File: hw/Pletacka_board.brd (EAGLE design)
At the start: 75 x 55 mm, 52 parts, among them U1 LM75BDP-NEW, U2 EL357N(A)(TA)-G, U3 EL357N(A)(TA)-G, U4 EL357N(A)(TA)-G, U5 EL357N(A)(TA)-G, U6 TPS54231D

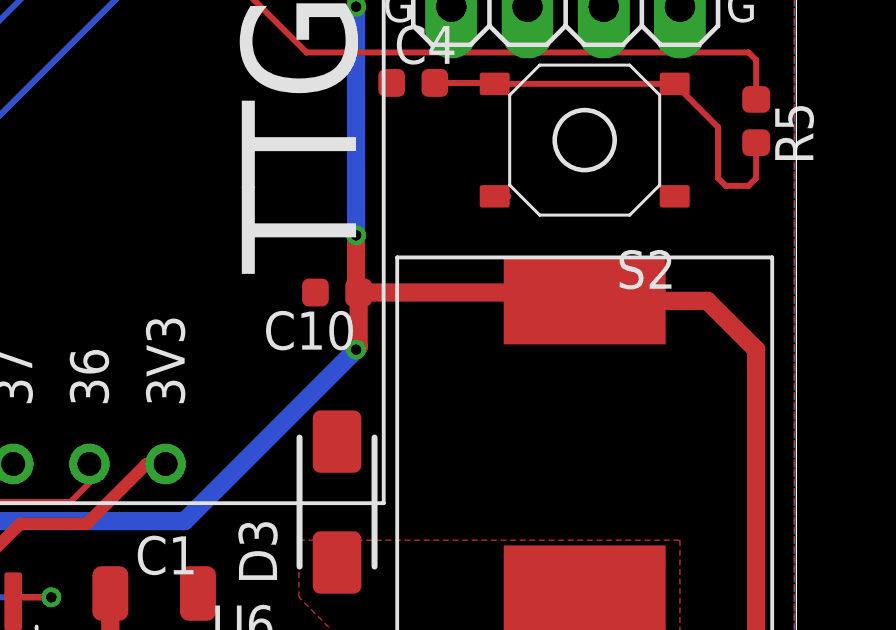
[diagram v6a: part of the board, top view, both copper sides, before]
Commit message: Change package of capacitor to 0805 (close #3)
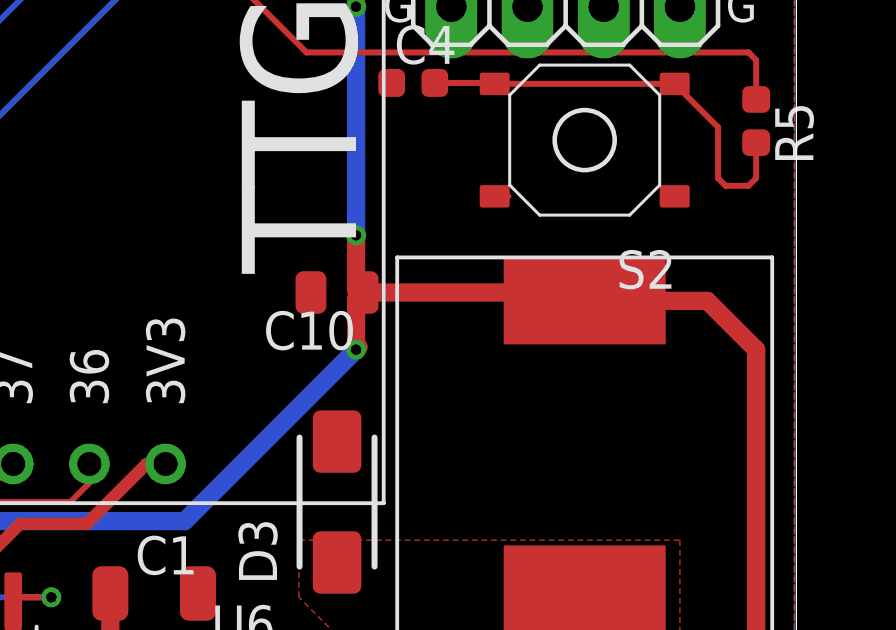
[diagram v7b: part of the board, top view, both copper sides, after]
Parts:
- C10: device rcl_upravena:C0603 -> rcl_upravena:C0805
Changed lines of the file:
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@@
 <attribute name="VALUE" x="67.31" y="17.78" size="1.27" layer="27" rot="R180"/>
 </element>
-<element name="C10" library="rcl_upravena" package="C0603" value="22u" x="59.69" y="31.115" smashed="yes" rot="R180">
-<attribute name="LCSC_ID" value="C59461" x="59.69" y="31.115" size="1.778" layer="27" rot="R180" display="off"/>
+<element name="C10" library="rcl_upravena" package="C0805" value="22u" x="59.69" y="31.115" smashed="yes" rot="R180">
+<attribute name="LCSC_ID" value="C45783" x="59.69" y="31.115" size="1.778" layer="27" rot="R180" display="off"/>
 <attribute name="NAME" x="60.325" y="30.48" size="1.27" layer="25" rot="R180"/>
 <attribute name="VALUE" x="60.325" y="33.02" size="1.27" layer="27" rot="R180"/>
@@
 <vertex x="0" y="0"/>
 </polygon>
-<wire x1="59.055" y1="31.03" x2="58.97" y2="31.115" width="0.1524" layer="1"/>
 <via x="59.055" y="17.145" extent="1-16" drill="0.65"/>
 <via x="59.055" y="15.24" extent="1-16" drill="0.65"/>
@@
 <via x="61.595" y="13.335" extent="1-16" drill="0.65"/>
 <via x="56.515" y="13.335" extent="1-16" drill="0.65"/>
+<wire x1="53.975" y1="48.26" x2="63.5" y2="52.705" width="0" layer="19" extent="1-1"/>
+<wire x1="51.435" y1="48.26" x2="53.975" y2="48.26" width="0" layer="19" extent="1-1"/>
+<wire x1="63.5" y1="40.64" x2="63.5" y2="52.705" width="0" layer="19" extent="1-1"/>
+<wire x1="66.04" y1="40.64" x2="63.5" y2="40.64" width="0" layer="19" extent="1-1"/>
+<wire x1="68.58" y1="40.64" x2="66.04" y2="40.64" width="0" layer="19" extent="1-1"/>
+<wire x1="71.12" y1="40.64" x2="68.58" y2="40.64" width="0" layer="19" extent="1-1"/>
+<wire x1="61.51" y1="38.1" x2="63.5" y2="40.64" width="0" layer="19" extent="1-1"/>
+<wire x1="64.945" y1="34.32" x2="61.51" y2="37.755" width="0" layer="19" extent="1-1"/>
+<wire x1="70.945" y1="34.32" x2="65.405" y2="34.32" width="0" layer="19" extent="1-1"/>
+<wire x1="58.82" y1="31.115" x2="64.945" y2="34.32" width="0" layer="19" extent="1-1"/>
+<wire x1="59.69" y1="26.145" x2="58.82" y2="31.115" width="0" layer="19" extent="1-1"/>
+<wire x1="55.054" y1="21.082" x2="59.69" y2="26.145" width="0" layer="19" extent="1-1"/>
+<wire x1="50.165" y1="20.955" x2="55.054" y2="21.082" width="0" layer="19" extent="1-1"/>
+<wire x1="28.575" y1="25.4" x2="28.575" y2="20.82" width="0" layer="19" extent="1-1"/>
+<wire x1="59.055" y1="17.145" x2="55.054" y2="21.082" width="0" layer="19" extent="1-1"/>
+<wire x1="61.525" y1="17.145" x2="59.055" y2="17.145" width="0" layer="19" extent="1-1"/>
+<wire x1="64.05" y1="17.145" x2="61.525" y2="17.145" width="0" layer="19" extent="1-1"/>
+<wire x1="61.595" y1="13.335" x2="59.055" y2="13.335" width="0" layer="19" extent="1-1"/>
+<wire x1="56.515" y1="13.335" x2="53.975" y2="13.25" width="0" layer="19" extent="1-1"/>
+<wire x1="2.032" y1="33.232" x2="2.08" y2="26.065" width="0" layer="19" extent="1-1"/>
+<wire x1="2.905" y1="42.103" x2="3.175" y2="34.925" width="0" layer="19" extent="1-1"/>
+<wire x1="2.905" y1="42.855" x2="2.905" y2="43.505" width="0" layer="19" extent="1-1"/>
+<wire x1="1.905" y1="45.1104" x2="2.905" y2="43.505" width="0" layer="19" extent="1-1"/>
+<wire x1="7.255" y1="44.257" x2="2.905" y2="43.505" width="0" layer="19" extent="1-1"/>
+<wire x1="31.115" y1="48.26" x2="51.435" y2="48.26" width="0" layer="19" extent="1-1"/>
+<wire x1="28.575" y1="48.26" x2="31.115" y2="48.26" width="0" layer="19" extent="1-1"/>
 </signal>
 <signal name="+3V3">
@@
 <wire x1="72.035" y1="30.835" x2="73.66" y2="29.21" width="0.6096" layer="1"/>
 <wire x1="73.66" y1="29.21" x2="73.66" y2="14.605" width="0.6096" layer="1"/>
-<wire x1="60.41" y1="31.115" x2="68.3" y2="31.115" width="0.6096" layer="1"/>
+<wire x1="60.56" y1="31.115" x2="68.3" y2="31.115" width="0.6096" layer="1"/>
 <wire x1="68.3" y1="31.115" x2="68.58" y2="30.835" width="0.6096" layer="1"/>
-<wire x1="60.41" y1="31.115" x2="60.41" y2="29.295" width="0.6096" layer="1"/>
 <wire x1="60.41" y1="29.295" x2="60.325" y2="29.21" width="0.6096" layer="1"/>
 <via x="60.325" y="29.21" extent="1-16" drill="0.35"/>
@@
 <wire x1="54.61" y1="23.495" x2="27.94" y2="23.495" width="0.6096" layer="16"/>
 <contactref element="JP1" pad="3"/>
-<wire x1="60.41" y1="31.115" x2="60.325" y2="31.2" width="0.6096" layer="1"/>
 <wire x1="60.325" y1="31.2" x2="60.325" y2="33.02" width="0.6096" layer="1"/>
 <via x="60.325" y="33.02" extent="1-16" drill="0.35"/>
@@
 <wire x1="60.325" y1="44.45" x2="60.325" y2="40.64" width="0.6096" layer="1"/>
 <wire x1="60.325" y1="44.45" x2="63.5" y2="47.625" width="0.6096" layer="1"/>
+<wire x1="60.325" y1="29.21" x2="60.325" y2="30.88" width="0.6096" layer="1"/>
+<wire x1="60.325" y1="30.88" x2="60.56" y2="31.115" width="0.6096" layer="1"/>
+<wire x1="60.56" y1="31.115" x2="60.325" y2="31.2" width="0" layer="19" extent="1-1"/>
 </signal>
 <signal name="TMP_SDA">

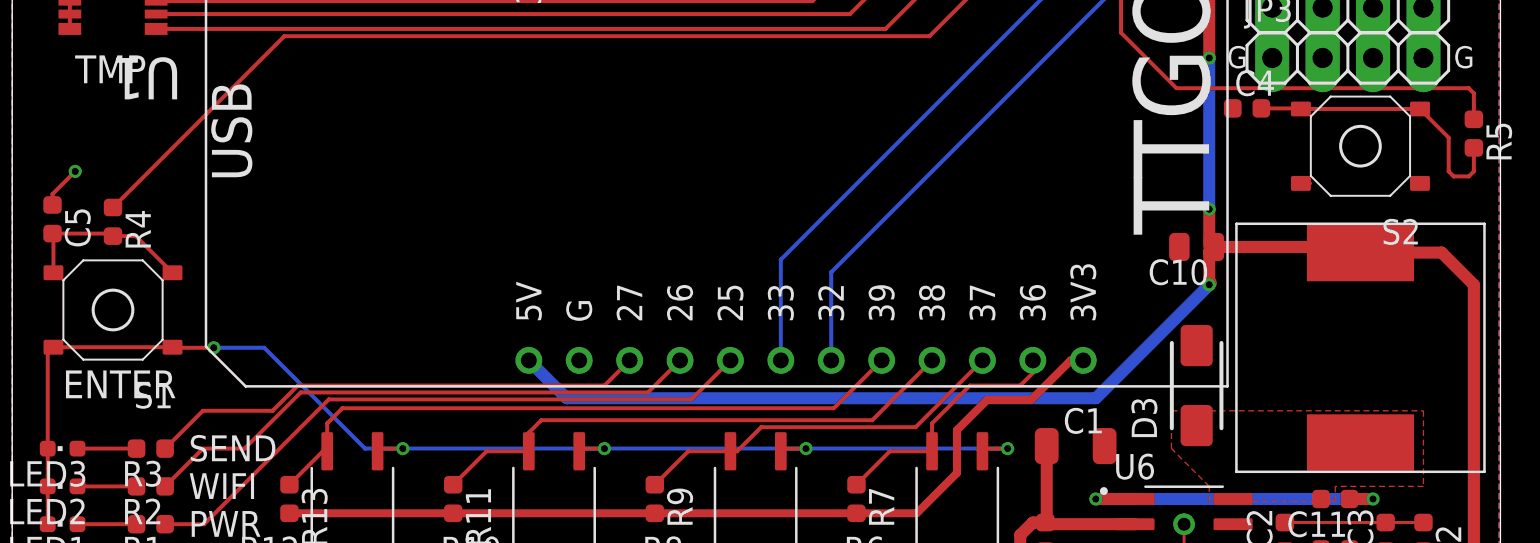
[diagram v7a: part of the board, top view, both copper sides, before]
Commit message: Edit buttons lables (close #16)
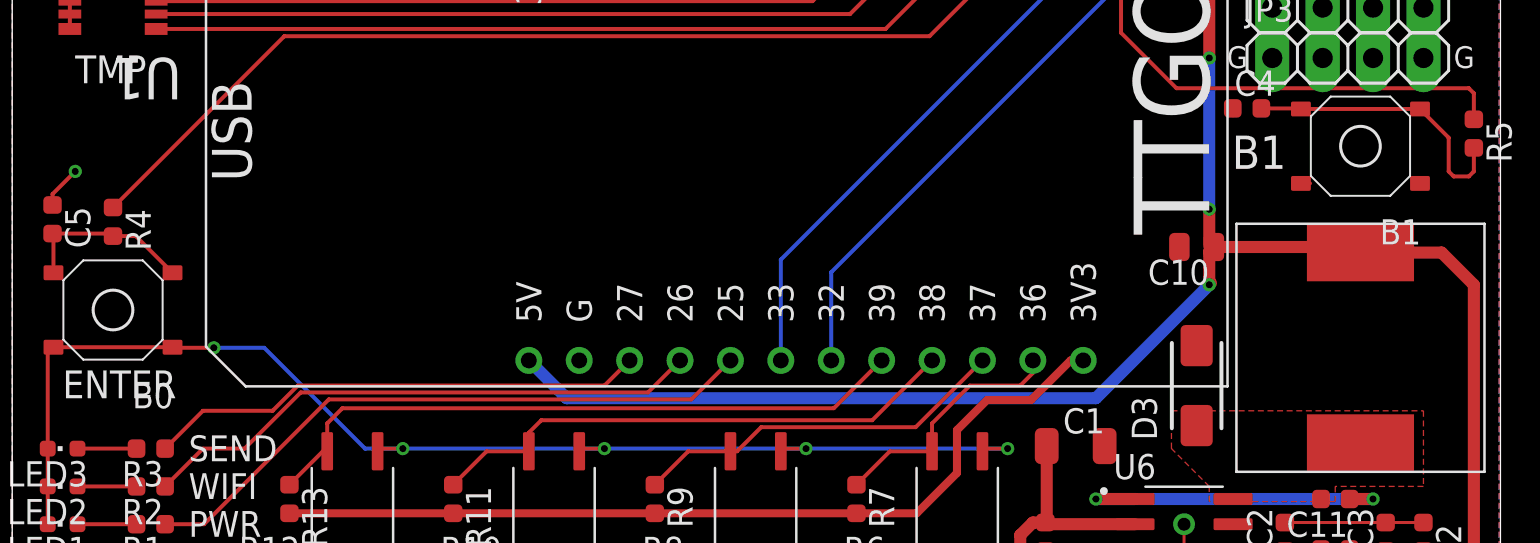
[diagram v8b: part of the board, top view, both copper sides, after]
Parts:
- B0: value CHOOSE_ME -> ENTER
- B1: value CHOOSE_ME -> B1
- renumbered S1 to B0, S2 to B1
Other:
- board text added: "B1"
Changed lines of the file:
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@@
 <drawing>
 <settings>
-<setting alwaysvectorfont="no"/>
+<setting alwaysvectorfont="yes"/>
 <setting verticaltext="up"/>
 </settings>
@@
 <text x="72.644" y="40.132" size="1.1" layer="21" font="vector" ratio="20" rot="SR0">G</text>
 <text x="61.214" y="40.132" size="1.1" layer="21" font="vector" ratio="20" rot="SR0">G</text>
+<text x="61.468" y="35.052" size="1.6764" layer="21" font="vector" ratio="20" rot="SR0">B1</text>
 </plain>
 <attributes>
@@
 <attribute name="LCSC_ID" value="C169399" x="67.945" y="26.035" size="1.778" layer="27" rot="R90" display="off"/>
 </element>
-<element name="S1" library="switch-omron" package="TS-1187A" value="CHOOSE_ME" x="5.08" y="27.94" smashed="yes" rot="R180">
+<element name="B0" library="switch-omron" package="TS-1187A" value="ENTER" x="5.08" y="27.94" smashed="yes" rot="R180">
 <attribute name="LCSC_ID" value="C318888" x="5.08" y="27.94" size="1.778" layer="27" rot="R180" display="off"/>
 <attribute name="NAME" x="8.128" y="24.257" size="1.27" layer="25" ratio="10" rot="R180"/>
 <attribute name="VALUE" x="8.128" y="33.02" size="1.27" layer="27" ratio="10" rot="R180"/>
 </element>
-<element name="S2" library="switch-omron" package="TS-1187A" value="CHOOSE_ME" x="67.945" y="36.195" smashed="yes" rot="R180">
+<element name="B1" library="switch-omron" package="TS-1187A" value="B1" x="67.945" y="36.195" smashed="yes" rot="R180">
 <attribute name="LCSC_ID" value="C318888" x="67.945" y="36.195" size="1.778" layer="27" rot="R180" display="off"/>
 <attribute name="NAME" x="70.993" y="32.512" size="1.27" layer="25" ratio="10" rot="R180"/>
@@
 <contactref element="U1" pad="5"/>
 <contactref element="C5" pad="1"/>
-<contactref element="S1" pad="A"/>
-<contactref element="S1" pad="B"/>
-<contactref element="S2" pad="A"/>
-<contactref element="S2" pad="B"/>
+<contactref element="B0" pad="A"/>
+<contactref element="B0" pad="B"/>
+<contactref element="B1" pad="A"/>
+<contactref element="B1" pad="B"/>
 <polygon width="0.6096" layer="1" rank="2">
 <vertex x="0" y="55"/>
@@
 <vertex x="0" y="0"/>
 </polygon>
+<wire x1="59.055" y1="31.03" x2="58.82" y2="31.115" width="0.1524" layer="1"/>
 <via x="59.055" y="17.145" extent="1-16" drill="0.65"/>
 <via x="59.055" y="15.24" extent="1-16" drill="0.65"/>
@@
 <wire x1="64.945" y1="34.32" x2="61.51" y2="37.755" width="0" layer="19" extent="1-1"/>
 <wire x1="70.945" y1="34.32" x2="65.405" y2="34.32" width="0" layer="19" extent="1-1"/>
-<wire x1="58.82" y1="31.115" x2="64.945" y2="34.32" width="0" layer="19" extent="1-1"/>
-<wire x1="59.69" y1="26.145" x2="58.82" y2="31.115" width="0" layer="19" extent="1-1"/>
+<wire x1="59.055" y1="31.03" x2="64.945" y2="34.32" width="0" layer="19" extent="1-1"/>
+<wire x1="59.69" y1="26.145" x2="59.055" y2="31.03" width="0" layer="19" extent="1-1"/>
 <wire x1="55.054" y1="21.082" x2="59.69" y2="26.145" width="0" layer="19" extent="1-1"/>
 <wire x1="50.165" y1="20.955" x2="55.054" y2="21.082" width="0" layer="19" extent="1-1"/>
@@
 <contactref element="R4" pad="2"/>
 <contactref element="C5" pad="2"/>
-<contactref element="S1" pad="C"/>
-<contactref element="S1" pad="D"/>
+<contactref element="B0" pad="C"/>
+<contactref element="B0" pad="D"/>
 <wire x1="2.032" y1="31.792" x2="2.08" y2="31.744" width="0.2" layer="1"/>
 <wire x1="2.08" y1="31.744" x2="2.08" y2="29.815" width="0.2" layer="1"/>
@@
 <contactref element="R5" pad="2"/>
 <contactref element="C4" pad="2"/>
-<contactref element="S2" pad="C"/>
-<contactref element="S2" pad="D"/>
+<contactref element="B1" pad="C"/>
+<contactref element="B1" pad="D"/>
 <wire x1="64.945" y1="38.07" x2="70.945" y2="38.07" width="0.2" layer="1"/>
 <wire x1="62.95" y1="38.1" x2="64.945" y2="38.1" width="0.2" layer="1"/>
